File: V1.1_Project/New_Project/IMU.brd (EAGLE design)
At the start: 160 x 100 mm, 60 parts, among them IC1 TC7660SEOA, IC2 AD8677AUJZ-REEL7, IC3 INA118U_2K5, U1 AZ1117EH-3.3TRG1

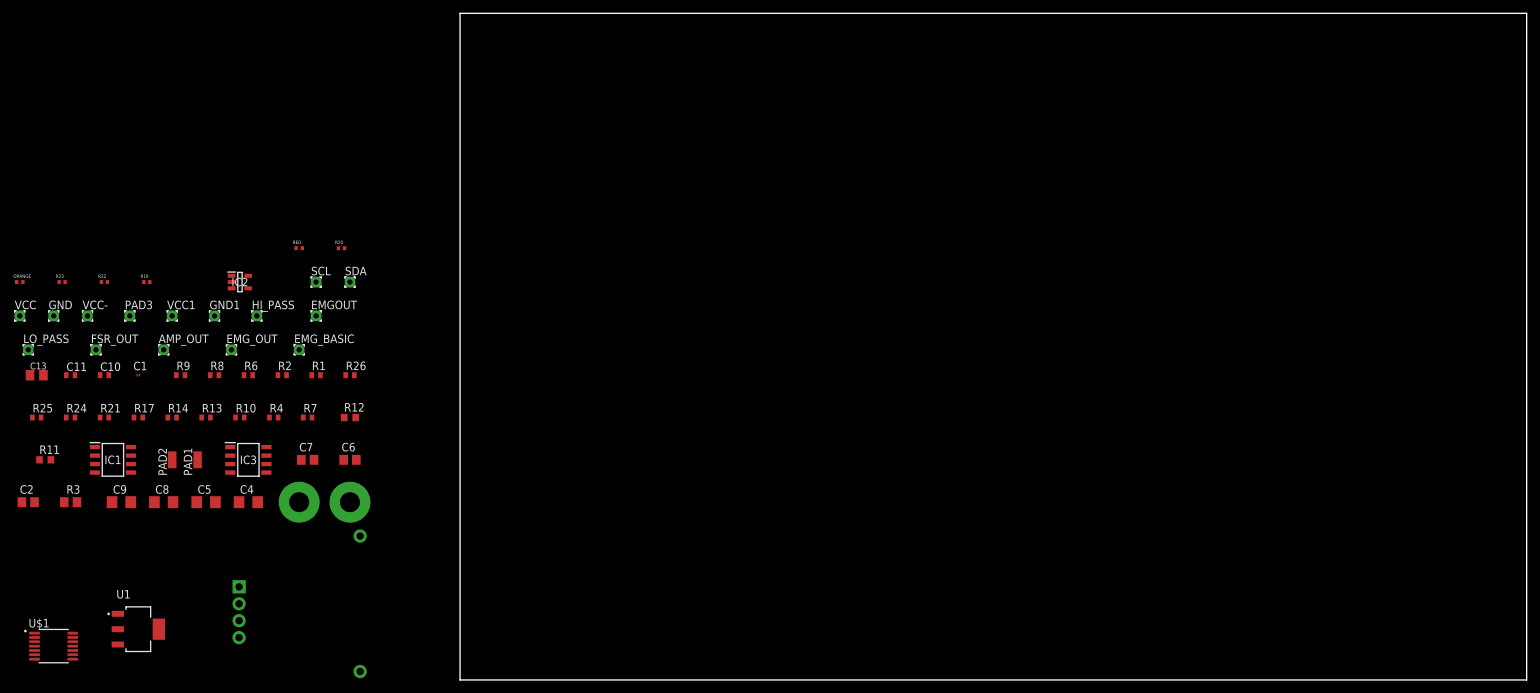
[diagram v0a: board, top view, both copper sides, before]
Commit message: Add files via upload
finished IMU layout including silkscreen
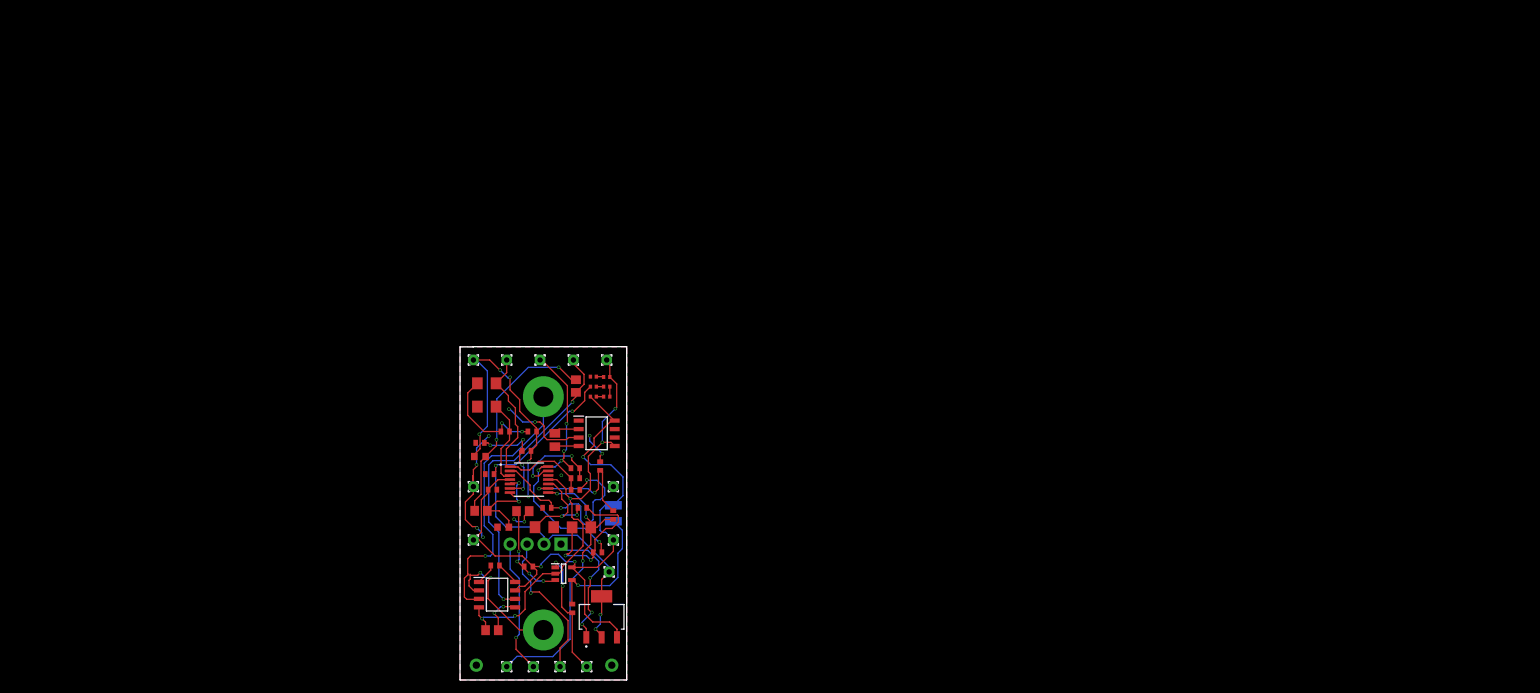
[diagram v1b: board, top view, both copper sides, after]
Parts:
- removed EMGOUT, EMG_BASIC: (no value), wirepad:1,6/0,8
- removed PAD3: (no value), wirepad@1:1,6/0,8
- removed R20: RESC0402X40N, RESC0402X40N:RESC0402X40N
- removed U$4: IMU, IMU:IMU
- added +3.3V, RAWEMG: (no value), wirepad:1,6/0,8
- added BLUE: RESC0402X40N, RESC0402X40N:RESC0402X40N
- added IMU: IMU, IMU:IMU
- C4, C5, C8, C9: device rcl@1:C1206 -> rcl:C1206
- C6, C7: device rcl@1:C0805 -> rcl:C0805
- R11: device adafruit@1:R0603 -> adafruit:R0603
- R12: device adafruit@2:R0603 -> adafruit@1:R0603
- R3: device rcl@1:R0805 -> rcl:R0805
- R4: device adafruit@2:R0402 -> adafruit@1:R0402
- R7: device adafruit@2:R1005 -> adafruit@1:R1005
- SCL, SDA: device wirepad@1:1,6/0,8 -> wirepad:1,6/0,8
- moved ORANGE 89.4 mm to (22.0, 44.0)
- moved R25 87.7 mm to (23.0, 24.8), turned to 90 degrees
- moved FSR_OUT 87.6 mm to (19.0, 2.00)
- moved R23 81.2 mm to (20.0, 44.0), turned to 180 degrees
- moved R24 80.5 mm to (16.8, 10.7), turned to 90 degrees
- moved C13 78.3 mm to (14.2, 36.0), turned to 270 degrees
- moved VCC- 78.2 mm to (22.0, 48.0)
- moved VCC 75.9 mm to (2.00, 21.0)
- moved U$1 75.6 mm to (10.3, 30.1)
- moved R22 75.3 mm to (20.0, 42.5), turned to 180 degrees
- moved VCC1 74.2 mm to (23.0, 21.0)
- moved IC1 72.7 mm to (20.5, 37.0)
- moved C2 72.2 mm to (4.78, 7.47)
- moved R17 71.8 mm to (20.6, 19.1)
- moved LO_PASS 71.8 mm to (7.00, 48.0)
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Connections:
- net +3.3V: now also +3.3V.1, IMU.+3.3V; no longer PAD3.1, U$4.+3.3V
- net -5V: now also BLUE.2; no longer R20.2
- net EMG_BASIC: no longer EMG_BASIC.1
- net GND: now also IMU.GND; no longer U$4.GND
- net N$16: now also IMU.SDA; no longer U$4.SDA
- net N$22: now also IMU.SCL; no longer U$4.SCL
- net N$6: now also BLUE.1; no longer R20.1
- net RAWEMG: now also RAWEMG.1; no longer EMGOUT.1
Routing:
- net +5V: track 0.00 -> 93.9 mm, vias 0 -> 3
- net -5V: track 0.00 -> 66.2 mm, vias 0 -> 5
- net GND: track 0.00 -> 65.3 mm, vias 0 -> 14
- net +3.3V: track 0.00 -> 62.8 mm, vias 0 -> 4
- net RAWEMG: track 0.00 -> 47.1 mm, vias 0 -> 2
- net PIN7: track 0.00 -> 46.4 mm, vias 0 -> 5
- net N$17: track 0.00 -> 44.2 mm, vias 0 -> 5
- net EMG_BASIC: track 0.00 -> 43.3 mm, vias 0 -> 3
- net N$5: track 0.00 -> 43.2 mm, vias 0 -> 1
- net N$23: track 0.00 -> 32.8 mm, vias 0 -> 2
- net N$14: track 0.00 -> 31.8 mm
- net N$19: track 0.00 -> 29.7 mm, vias 0 -> 2
- net N$16: track 0.00 -> 23.0 mm, vias 0 -> 1
- net N$27: track 0.00 -> 23.0 mm, vias 0 -> 2
- net N$7: track 0.00 -> 20.7 mm, vias 0 -> 1
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- added copper zone on layer 1, net GND
- added copper zone on layer 16, net GND
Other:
- board size 160 x 100 mm -> 25 x 50 mm
- board text added: "+3.3V"
- board text added: "-5V"
- board text added: "100K"
- board text added: "100R"
- board text added: "10pF"
- board text added: "10uF"
- board text added: "150R"
- board text added: "16K"
- board text added: "1K"
- board text added: "1uF"
- board text added: "22nF"
- board text added: "24K"
- board text added: "3.3V"
- board text added: "3.3nF"
- board text added: "390K"
- board text added: "4.7K"
- board text added: "51K"
- board text added: "5V"
- board text added: "68K"
- board text added: "75K"
- board text added: "787K"
- board text added: "AD8677 FSR"
- board text added: "AMP_OUT"
- board text added: "AZ1117 +3.3V"
- board text added: "EMG_OUT"
- board text added: "FSR_OUT"
- board text added: "GND"
- board text added: "HI_PASS"
- board text added: "INA118U EMG"
- board text added: "LO_PASS"
- board text added: "RAW_EMG"
- board text added: "SCL"
- board text added: "SDA"
- board text added: "TC7760 DC-DC"
- board text added: "TLC2274 4OpAmp"
- board text added: "VCC"
- board text added: "VCC-"
